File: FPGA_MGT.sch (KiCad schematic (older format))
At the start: 5 parts, among them U1 XC7K160T-FFG676

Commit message: REF CLK for MIG
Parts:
- removed R169, R61: R0201_100R_1%_0.05W_200PPM, RESC0603X28N, symbol Resistors_SMD:R0201_100R_1%_0.05W_200PPM
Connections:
- net labels removed: FPGA_REF_CLK1_N, FPGA_REF_CLK1_P
- wire segments 148 -> 143
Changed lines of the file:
@@
 Comment4 ""
 $EndDescr
-Text HLabel 9700 1200 2    50   Input ~ 10
-FPGA_REF_CLK1_N
-Text HLabel 9700 1100 2    50   Input ~ 10
-FPGA_REF_CLK1_P
 Text HLabel 9700 900  2    50   Input ~ 10
 FPGA_REF_CLK0_N
@@
 Text Label 9550 900  2    50   ~ 10
 FPGA_REF_CLK0_N
-Text Label 9550 1100 2    50   ~ 10
-FPGA_REF_CLK1_P
-Text Label 9550 1200 2    50   ~ 10
-FPGA_REF_CLK1_N
 Wire Wire Line
 	8600 800  9700 800
@@
 	8600 900  9700 900
 Wire Wire Line
-	8600 1100 9700 1100
-Wire Wire Line
-	8600 1200 9700 1200
-Wire Wire Line
 	8000 800  8000 900
-Wire Wire Line
-	8000 1100 8000 1200
 $Comp
 L power:GND #PWR?
@@
 	1    0    0    -1
 $EndComp
-$Comp
-L power:GND #PWR?
-U 1 1 5FFB2211
-P 8000 1200
-AR Path="/5BD32060/5FFB2211" Ref="#PWR?"  Part="1"
-AR Path="/5BABAC65/5FFB2211" Ref="#PWR?"  Part="1"
-AR Path="/5CC24E97/5FFB2211" Ref="#PWR?"  Part="1"
-AR Path="/5CC393D3/5FFB2211" Ref="#PWR?"  Part="1"
-AR Path="/5CC6DBF7/5FFB2211" Ref="#PWR?"  Part="1"
-AR Path="/5CC8AFE1/5FFB2211" Ref="#PWR?"  Part="1"
-AR Path="/5C907554/5C417BCB/5FFB2211" Ref="#PWR?"  Part="1"
-AR Path="/5C907554/5DCA928C/5FFB2211" Ref="#PWR0494"  Part="1"
-F 0 "#PWR0494" H 8000 950 50  0001 C CNN
-F 1 "GND" H 8005 1027 50  0000 C CNN
-F 2 "" H 8000 1200 50  0001 C CNN
-F 3 "" H 8000 1200 50  0001 C CNN
-	1    8000 1200
-	1    0    0    -1
-$EndComp
 Wire Wire Line
 	8000 800  8300 800
@@
 	8000 900  8300 900
 Connection ~ 8000 900
-Wire Wire Line
-	8000 1100 8300 1100
-Wire Wire Line
-	8000 1200 8300 1200
-Connection ~ 8000 1200
 $Comp
 L Resistors_SMD:R0201_100R_1%_0.05W_200PPM R59
@@
 	1    0    0    -1
 $EndComp
-$Comp
-L Resistors_SMD:R0201_100R_1%_0.05W_200PPM R61
-U 1 1 5DCB78D4
-P 8300 1100
-F 0 "R61" H 8300 1150 50  0000 C CNN
-F 1 "R0201_100R_1%_0.05W_200PPM" H 8300 890 60  0001 L CNN
-F 2 "RESC0603X28N" H 8300 80  60  0001 L CNN
-F 3 "\\\\cern.ch\\dfs\\Applications\\Altium\\Datasheets\\R0201_VISHAY_CRCW e3.pdf" H 8300 710 60  0001 L CNN
-F 4 "200" H 8650 1150 50  0000 C CNN "~"
-F 5 "R0201_200R_1%_0.05W_200PPM" H 8300 620 60  0001 L CNN "Part Number"
-F 6 "Resistor - 1%" H 8300 530 60  0001 L CNN "Library Ref"
-F 7 "SchLib\\Resistors.SchLib" H 8300 440 60  0001 L CNN "Library Path"
-F 8 "=Value" H 8300 350 60  0001 L CNN "Comment"
-F 9 "Standard" H 8300 260 60  0001 L CNN "Component Kind"
-F 10 "Standard" H 8300 170 60  0001 L CNN "Component Type"
-F 11 "~~" H 8300 -10 60  0001 L CNN "PackageDescription"
-F 12 "2" H 8300 -100 60  0001 L CNN "Pin Count"
-F 13 "PcbLib\\Resistors SMD.PcbLib" H 8300 -190 60  0001 L CNN "Footprint Path"
-F 14 "RESC0603X28N" H 8300 -280 60  0001 L CNN "Footprint Ref"
-F 15 "100" H 8300 -370 60  0001 L CNN "Val"
-F 16 "Not Recommended" H 8300 -460 60  0001 L CNN "Status"
-F 17 "0.05W" H 8300 -550 60  0001 L CNN "Power"
-F 18 "±200ppm/°C" H 8300 -640 60  0001 L CNN "TC"
-F 19 "~~" H 8300 -730 60  0001 L CNN "Voltage"
-F 20 "±1%" H 8300 -820 60  0001 L CNN "Tolerance"
-F 21 "Thick Film Chip Resistor" H 8300 -910 60  0001 L CNN "Part Description"
-F 22 "GENERIC" H 8300 -1000 60  0001 L CNN "Manufacturer"
-F 23 "R0201_200R_1%_0.05W_200PPM" H 8300 -1090 60  0001 L CNN "Manufacturer Part Number"
-F 24 "0201" H 8300 -1180 60  0001 L CNN "Case"
-F 25 "No" H 8300 -1270 60  0001 L CNN "PressFit"
-F 26 "Yes" H 8300 -1360 60  0001 L CNN "Mounted"
-F 27 "~~" H 8300 -1450 60  0001 L CNN "Sense Comment"
-F 28 "No" H 8300 -1540 60  0001 L CNN "Sense"
-F 29 "~~" H 8300 -1630 60  0001 L CNN "Status Comment"
-F 30 "No" H 8300 -1720 60  0001 L CNN "Socket"
-F 31 "Yes" H 8300 -1810 60  0001 L CNN "SMD"
-F 32 "~~" H 8300 -1900 60  0001 L CNN "ComponentHeight"
-F 33 "VISHAY" H 8300 -1990 60  0001 L CNN "Manufacturer1 Example"
-F 34 "CRCW0201200RFNED" H 8300 -2080 60  0001 L CNN "Manufacturer1 Part Number"
-F 35 "0.27mm" H 8300 -2170 60  0001 L CNN "Manufacturer1 ComponentHeight"
-F 36 "\\\\cern.ch\\dfs\\Applications\\Altium\\Datasheets\\R0201_VISHAY_CRCW e3.pdf" H 8300 -2260 60  0001 L CNN "HelpURL"
-F 37 "CERN DEM JLC" H 8300 -2350 60  0001 L CNN "Author"
-F 38 "11/13/14 00:00:00" H 8300 -2440 60  0001 L CNN "CreateDate"
-F 39 "11/13/14 00:00:00" H 8300 -2530 60  0001 L CNN "LatestRevisionDate"
-F 40 "Resistors SMD" H 8300 -2620 60  0001 L CNN "Library Name"
-F 41 "This work is licensed under the Creative Commons CC-BY-SA 4.0 License. To the extent that circuit schematics that use Licensed Material can be considered to be ‘Adapted Material’, then the copyright holder waives article 3.b of the license with respect to these schematics." H 8300 -2710 60  0001 L CNN "License"
-	1    8300 1100
-	1    0    0    -1
-$EndComp
-$Comp
-L Resistors_SMD:R0201_100R_1%_0.05W_200PPM R169
-U 1 1 5DCC9ABA
-P 8300 1200
-F 0 "R169" H 8300 1250 50  0000 C CNN
-F 1 "R0201_100R_1%_0.05W_200PPM" H 8300 990 60  0001 L CNN
-F 2 "RESC0603X28N" H 8300 180 60  0001 L CNN
-F 3 "\\\\cern.ch\\dfs\\Applications\\Altium\\Datasheets\\R0201_VISHAY_CRCW e3.pdf" H 8300 810 60  0001 L CNN
-F 4 "200" H 8650 1250 50  0000 C CNN "~"
-F 5 "R0201_200R_1%_0.05W_200PPM" H 8300 720 60  0001 L CNN "Part Number"
-F 6 "Resistor - 1%" H 8300 630 60  0001 L CNN "Library Ref"
-F 7 "SchLib\\Resistors.SchLib" H 8300 540 60  0001 L CNN "Library Path"
-F 8 "=Value" H 8300 450 60  0001 L CNN "Comment"
-F 9 "Standard" H 8300 360 60  0001 L CNN "Component Kind"
-F 10 "Standard" H 8300 270 60  0001 L CNN "Component Type"
-F 11 "~~" H 8300 90  60  0001 L CNN "PackageDescription"
-F 12 "2" H 8300 0   60  0001 L CNN "Pin Count"
-F 13 "PcbLib\\Resistors SMD.PcbLib" H 8300 -90 60  0001 L CNN "Footprint Path"
-F 14 "RESC0603X28N" H 8300 -180 60  0001 L CNN "Footprint Ref"
-F 15 "100" H 8300 -270 60  0001 L CNN "Val"
-F 16 "Not Recommended" H 8300 -360 60  0001 L CNN "Status"
-F 17 "0.05W" H 8300 -450 60  0001 L CNN "Power"
-F 18 "±200ppm/°C" H 8300 -540 60  0001 L CNN "TC"
-F 19 "~~" H 8300 -630 60  0001 L CNN "Voltage"
-F 20 "±1%" H 8300 -720 60  0001 L CNN "Tolerance"
-F 21 "Thick Film Chip Resistor" H 8300 -810 60  0001 L CNN "Part Description"
-F 22 "GENERIC" H 8300 -900 60  0001 L CNN "Manufacturer"
-F 23 "R0201_200R_1%_0.05W_200PPM" H 8300 -990 60  0001 L CNN "Manufacturer Part Number"
-F 24 "0201" H 8300 -1080 60  0001 L CNN "Case"
-F 25 "No" H 8300 -1170 60  0001 L CNN "PressFit"
-F 26 "Yes" H 8300 -1260 60  0001 L CNN "Mounted"
-F 27 "~~" H 8300 -1350 60  0001 L CNN "Sense Comment"
-F 28 "No" H 8300 -1440 60  0001 L CNN "Sense"
-F 29 "~~" H 8300 -1530 60  0001 L CNN "Status Comment"
-F 30 "No" H 8300 -1620 60  0001 L CNN "Socket"
-F 31 "Yes" H 8300 -1710 60  0001 L CNN "SMD"
-F 32 "~~" H 8300 -1800 60  0001 L CNN "ComponentHeight"
-F 33 "VISHAY" H 8300 -1890 60  0001 L CNN "Manufacturer1 Example"
-F 34 "CRCW0201200RFNED" H 8300 -1980 60  0001 L CNN "Manufacturer1 Part Number"
-F 35 "0.27mm" H 8300 -2070 60  0001 L CNN "Manufacturer1 ComponentHeight"
-F 36 "\\\\cern.ch\\dfs\\Applications\\Altium\\Datasheets\\R0201_VISHAY_CRCW e3.pdf" H 8300 -2160 60  0001 L CNN "HelpURL"
-F 37 "CERN DEM JLC" H 8300 -2250 60  0001 L CNN "Author"
-F 38 "11/13/14 00:00:00" H 8300 -2340 60  0001 L CNN "CreateDate"
-F 39 "11/13/14 00:00:00" H 8300 -2430 60  0001 L CNN "LatestRevisionDate"
-F 40 "Resistors SMD" H 8300 -2520 60  0001 L CNN "Library Name"
-F 41 "This work is licensed under the Creative Commons CC-BY-SA 4.0 License. To the extent that circuit schematics that use Licensed Material can be considered to be ‘Adapted Material’, then the copyright holder waives article 3.b of the license with respect to these schematics." H 8300 -2610 60  0001 L CNN "License"
-	1    8300 1200
-	1    0    0    -1
-$EndComp

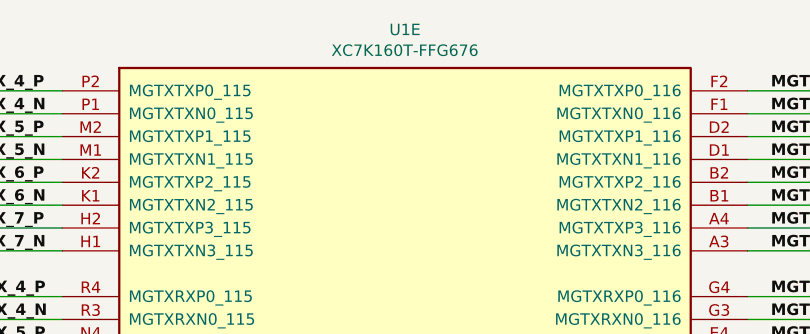
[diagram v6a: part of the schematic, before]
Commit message: PN updated for some components, README_fab.txt updated
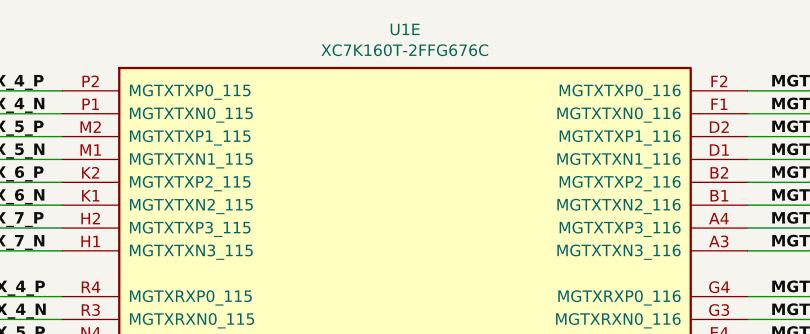
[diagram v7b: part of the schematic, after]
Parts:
- U1: value XC7K160T-FFG676 -> XC7K160T-2FFG676C
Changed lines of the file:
@@
 P 2750 1950
 F 0 "U1" H 2750 3317 50  0000 C CNN
-F 1 "XC7K160T-FFG676" H 2750 3226 50  0000 C CNN
+F 1 "XC7K160T-2FFG676C" H 2750 3226 50  0000 C CNN
 F 2 "ICs And Semiconductors SMD_BGA:BGA676C100P26X26_2700X2700X260" H 2750 1950 50  0001 C CNN
 F 3 "" H 2750 1950 50  0000 C CNN

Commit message: Automated edit to move cache / rescue symbols to actual eeschem library
Results of running dissect_lib3.py, not posted here
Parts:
- U1: symbol FPGA_Xilinx_Kintex7:XC7K160T-FFG676 -> marble_misc:XC7K160T-FFG676
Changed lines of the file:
@@
 $EndComp
 $Comp
-L FPGA_Xilinx_Kintex7:XC7K160T-FFG676 U1
+L marble_misc:XC7K160T-FFG676 U1
 U 5 1 5F2C6FBA
 P 2750 1950
